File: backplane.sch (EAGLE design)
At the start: 8 parts, among them J1 5535070-4, J2 5535070-4, J3 5535070-4, J4 5535070-4, J5 5535070-4, J6 5535070-4, J7 5535070-4, J8 5535070-4

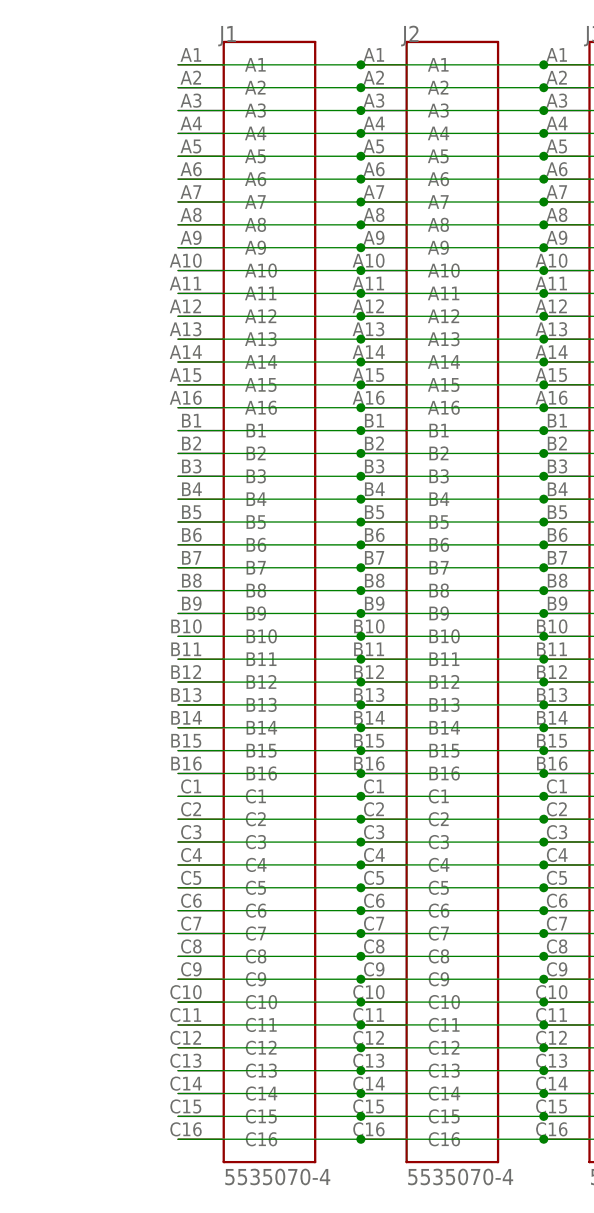
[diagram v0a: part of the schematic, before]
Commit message: routed the wires between backplane connectors, and alligned them with the centers
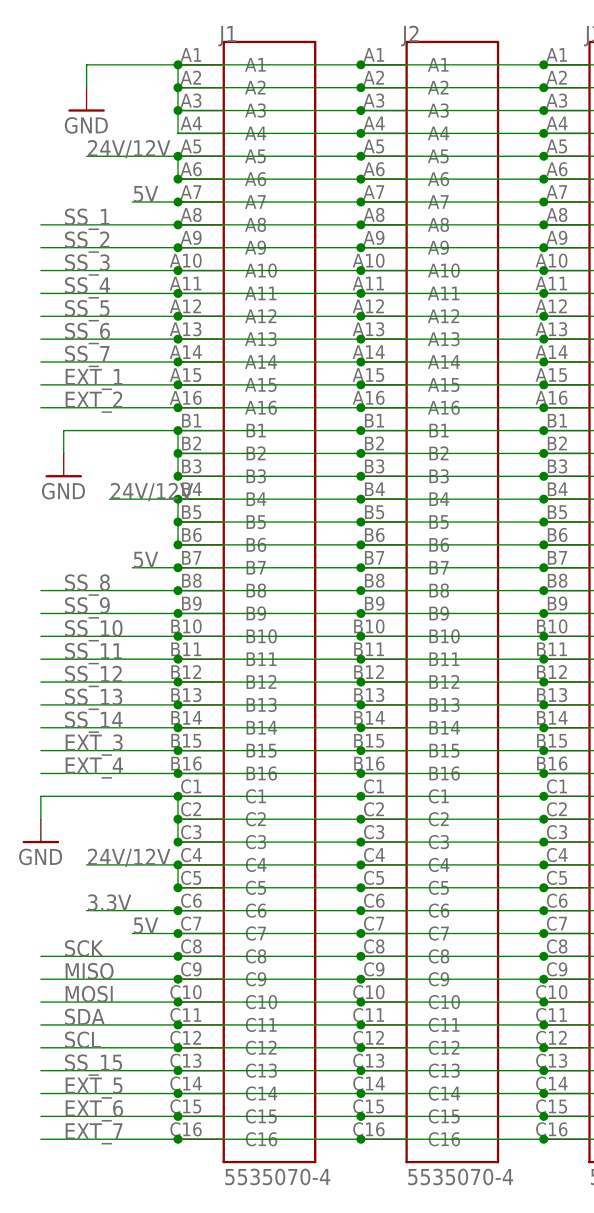
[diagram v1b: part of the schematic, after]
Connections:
- net N$10 renamed SS_3
- net N$11 renamed SS_5
- net N$12 renamed SS_4
- net N$13 renamed SS_6
- net N$14 renamed SS_7
- net N$15 renamed EXT_1
- net N$17 renamed EXT_2
- net N$24 renamed SS_8
- net N$25 renamed SS_9
- net N$26 renamed SS_10
- net N$27 renamed SS_11
- net N$28 renamed SS_12
- net N$29 renamed SS_13
- net N$30 renamed SS_14
- net N$31 renamed EXT_3
- net N$32 renamed EXT_4
- net N$38 renamed 3.3V
- net N$40 renamed SCK
- net N$41 renamed MISO
- net N$42 renamed MOSI
- net N$43 renamed SDA
- net N$44 renamed SCL
- net N$45 renamed SS_15
- net N$46 renamed EXT_5
- net N$47 renamed EXT_6
- net N$48 renamed EXT_7
- net N$8 renamed SS_1
- net N$9 renamed SS_2
- removed net N$1: J1.A1, J2.A1, J3.A1, J4.A1, J5.A1, J6.A1, J7.A1, J8.A1
- removed net N$16: J1.B1, J2.B1, J3.B1, J4.B1, J5.B1, J6.B1, J7.B1, J8.B1
- removed net N$18: J1.B2, J2.B2, J3.B2, J4.B2, J5.B2, J6.B2, J7.B2, J8.B2
- removed net N$19: J1.B3, J2.B3, J3.B3, J4.B3, J5.B3, J6.B3, J7.B3, J8.B3
- removed net N$2: J1.A2, J2.A2, J3.A2, J4.A2, J5.A2, J6.A2, J7.A2, J8.A2
- removed net N$20: J1.B4, J2.B4, J3.B4, J4.B4, J5.B4, J6.B4, J7.B4, J8.B4
- removed net N$21: J1.B5, J2.B5, J3.B5, J4.B5, J5.B5, J6.B5, J7.B5, J8.B5
- removed net N$22: J1.B6, J2.B6, J3.B6, J4.B6, J5.B6, J6.B6, J7.B6, J8.B6
- removed net N$23: J1.B7, J2.B7, J3.B7, J4.B7, J5.B7, J6.B7, J7.B7, J8.B7
- removed net N$3: J1.A3, J2.A3, J3.A3, J4.A3, J5.A3, J6.A3, J7.A3, J8.A3
- removed net N$33: J1.C1, J2.C1, J3.C1, J4.C1, J5.C1, J6.C1, J7.C1, J8.C1
- removed net N$34: J1.C2, J2.C2, J3.C2, J4.C2, J5.C2, J6.C2, J7.C2, J8.C2
- removed net N$35: J1.C3, J2.C3, J3.C3, J4.C3, J5.C3, J6.C3, J7.C3, J8.C3
- removed net N$36: J1.C4, J2.C4, J3.C4, J4.C4, J5.C4, J6.C4, J7.C4, J8.C4
- removed net N$37: J1.C5, J2.C5, J3.C5, J4.C5, J5.C5, J6.C5, J7.C5, J8.C5
- removed net N$39: J1.C7, J2.C7, J3.C7, J4.C7, J5.C7, J6.C7, J7.C7, J8.C7
- removed net N$4: J1.A4, J2.A4, J3.A4, J4.A4, J5.A4, J6.A4, J7.A4, J8.A4
- removed net N$5: J1.A5, J2.A5, J3.A5, J4.A5, J5.A5, J6.A5, J7.A5, J8.A5
- removed net N$6: J1.A6, J2.A6, J3.A6, J4.A6, J5.A6, J6.A6, J7.A6, J8.A6
- removed net N$7: J1.A7, J2.A7, J3.A7, J4.A7, J5.A7, J6.A7, J7.A7, J8.A7
- new net 24V/12V: J1.A5, J1.A6, J1.B4, J1.B5, J1.B6, J1.C4, J1.C5, J2.A5, J2.A6, J2.B4, J2.B5, J2.B6, J2.C4, J2.C5, J3.A5, J3.A6, J3.B4, J3.B5, J3.B6, J3.C4, J3.C5, J4.A5, J4.A6, J4.B4, J4.B5, J4.B6, J4.C4, J4.C5, J5.A5, J5.A6, J5.B4, J5.B5, J5.B6, J5.C4, J5.C5, J6.A5, J6.A6, J6.B4, J6.B5, J6.B6, J6.C4, J6.C5, J7.A5, J7.A6, J7.B4, J7.B5, J7.B6, J7.C4, J7.C5, J8.A5, J8.A6, J8.B4, J8.B5, J8.B6, J8.C4, J8.C5
- new net 5V: J1.A7, J1.B7, J1.C7, J2.A7, J2.B7, J2.C7, J3.A7, J3.B7, J3.C7, J4.A7, J4.B7, J4.C7, J5.A7, J5.B7, J5.C7, J6.A7, J6.B7, J6.C7, J7.A7, J7.B7, J7.C7, J8.A7, J8.B7, J8.C7
- new net GND: J1.A1, J1.A2, J1.A3, J1.A4, J1.B1, J1.B2, J1.B3, J1.C1, J1.C2, J1.C3, J2.A1, J2.A2, J2.A3, J2.A4, J2.B1, J2.B2, J2.B3, J2.C1, J2.C2, J2.C3, J3.A1, J3.A2, J3.A3, J3.A4, J3.B1, J3.B2, J3.B3, J3.C1, J3.C2, J3.C3, J4.A1, J4.A2, J4.A3, J4.A4, J4.B1, J4.B2, J4.B3, J4.C1, J4.C2, J4.C3, J5.A1, J5.A2, J5.A3, J5.A4, J5.B1, J5.B2, J5.B3, J5.C1, J5.C2, J5.C3, J6.A1, J6.A2, J6.A3, J6.A4, J6.B1, J6.B2, J6.B3, J6.C1, J6.C2, J6.C3, J7.A1, J7.A2, J7.A3, J7.A4, J7.B1, J7.B2, J7.B3, J7.C1, J7.C2, J7.C3, J8.A1, J8.A2, J8.A3, J8.A4, J8.B1, J8.B2, J8.B3, J8.C1, J8.C2, J8.C3

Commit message: finished backplane
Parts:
- added C1, C3: 10Uf, rc-master-smd:CP_3216
- added C2, C4: 10Uf, rc-master-smd:C_1206
- added JP2: (no value), pinhead:PINHD-2X15
- added U1: LM1084IS-5.0, LM1084IS-5.0:LM1084IS-5.0
- added U2: LM1084IS-3.3, LM1084IS-5.0:LM1084IS-5.0
- added XS1: (no value), con-dg55:2P
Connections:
- new net N$1: C3.+, U2.IN
- new net N$2: C1.+, U1.IN
- net 24V/12V: now also XS1.P$2
- net 3.3V: now also C4.2, JP2.5, U2.OUT, U2.VOUT
- net 5V: now also C2.2, JP2.3, U1.OUT, U1.VOUT
- net EXT_1: now also JP2.17
- net EXT_2: now also JP2.19
- net EXT_3: now also JP2.21
- net EXT_4: now also JP2.23
- net EXT_5: now also JP2.25
- net EXT_6: now also JP2.27
- net EXT_7: now also JP2.29
- net GND: now also C1.-, C2.1, C3.-, C4.1, JP2.1, U1.ADJ/GND, U2.ADJ/GND, XS1.P$1
- net MISO: now also JP2.9
- net MOSI: now also JP2.11
- net SCK: now also JP2.7
- net SCL: now also JP2.15
- net SDA: now also JP2.13
- net SS_1: now also JP2.30
- net SS_10: now also JP2.12
- net SS_11: now also JP2.10
- net SS_12: now also JP2.8
- net SS_13: now also JP2.6
- net SS_14: now also JP2.4
- net SS_15: now also JP2.2
- net SS_2: now also JP2.28
- net SS_3: now also JP2.26
- net SS_4: now also JP2.24
- net SS_5: now also JP2.22
- net SS_6: now also JP2.20
- net SS_7: now also JP2.18
- net SS_8: now also JP2.16
- net SS_9: now also JP2.14
